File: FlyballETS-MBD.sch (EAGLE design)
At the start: 16 parts, among them Q1 BC557, Q2 BC557

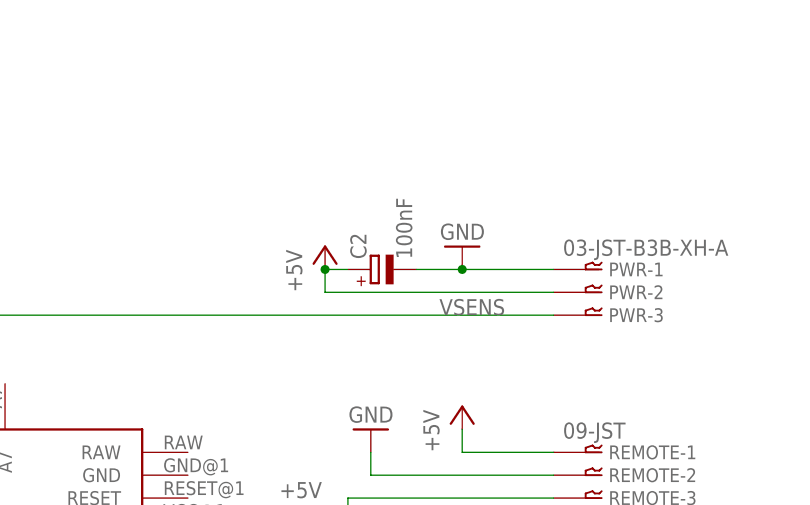
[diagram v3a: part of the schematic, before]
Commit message: Incorrect capacitor value
Changed 100nF to 100uF
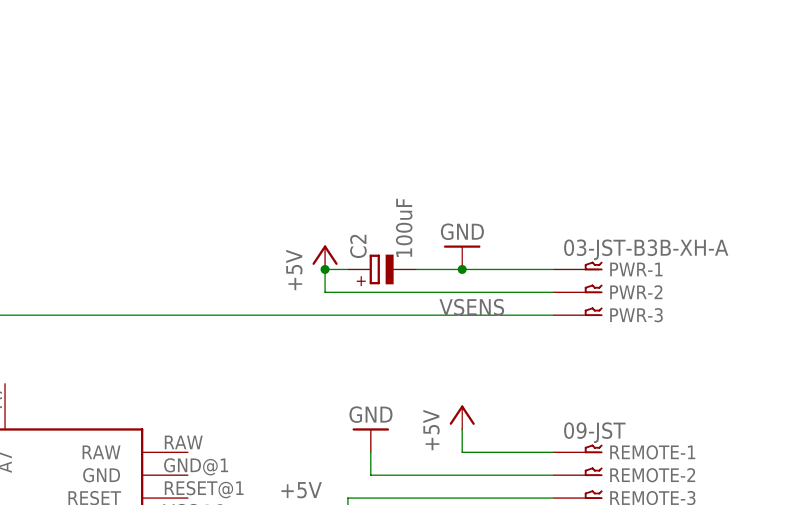
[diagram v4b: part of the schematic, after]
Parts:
- C2: value 100nF -> 100uF
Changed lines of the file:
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@@
 <part name="P+2" library="supply1" deviceset="+5V" device=""/>
 <part name="GND7" library="supply1" deviceset="GND" device=""/>
-<part name="C2" library="resistor" deviceset="CPOL-EU" device="E2,5-6E" value="100nF"/>
+<part name="C2" library="resistor" deviceset="CPOL-EU" device="E2,5-6E" value="100uF"/>
 <part name="ARDUINO" library="_custom" deviceset="ARDPROMINISOCK" device=""/>
 <part name="FRAME1" library="frames" deviceset="A4L-LOC" device=""/>

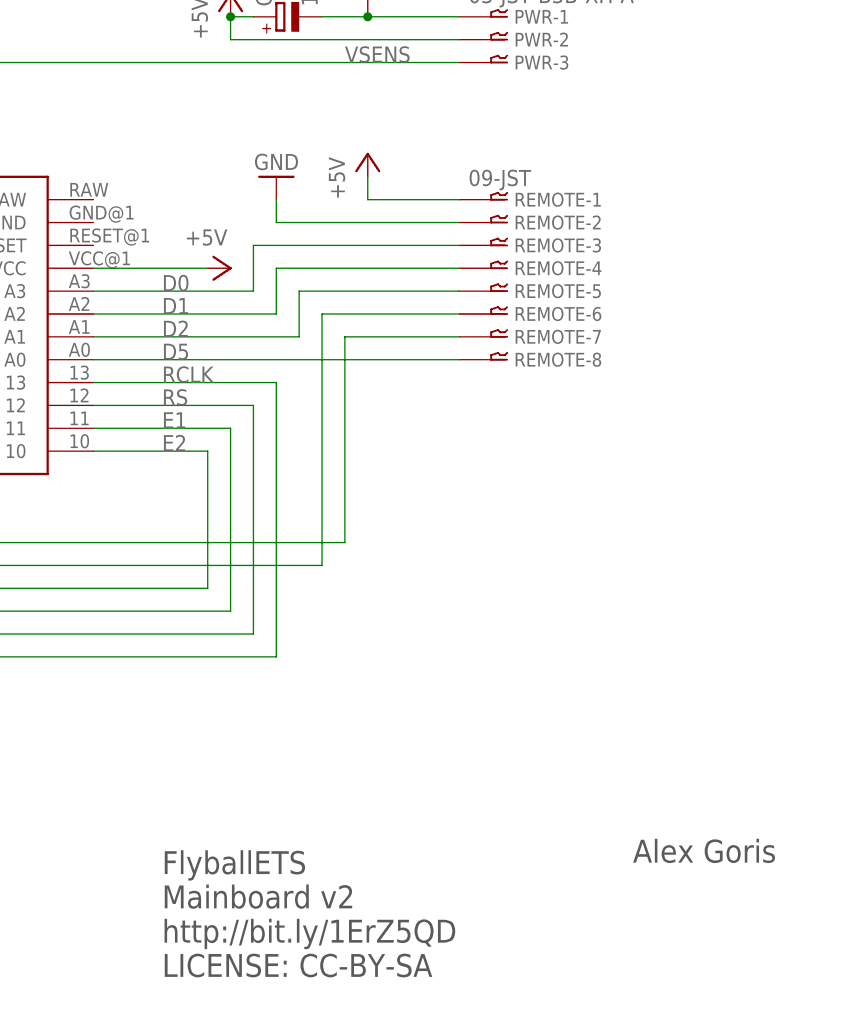
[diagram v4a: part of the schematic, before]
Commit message: Fixed JST XH pin numbering
Updated bt_con-jst-xh.lbr library with swapped pin numbering.
Updated all board designs with updated library so they have the
connectors the right way around
Fixes #4
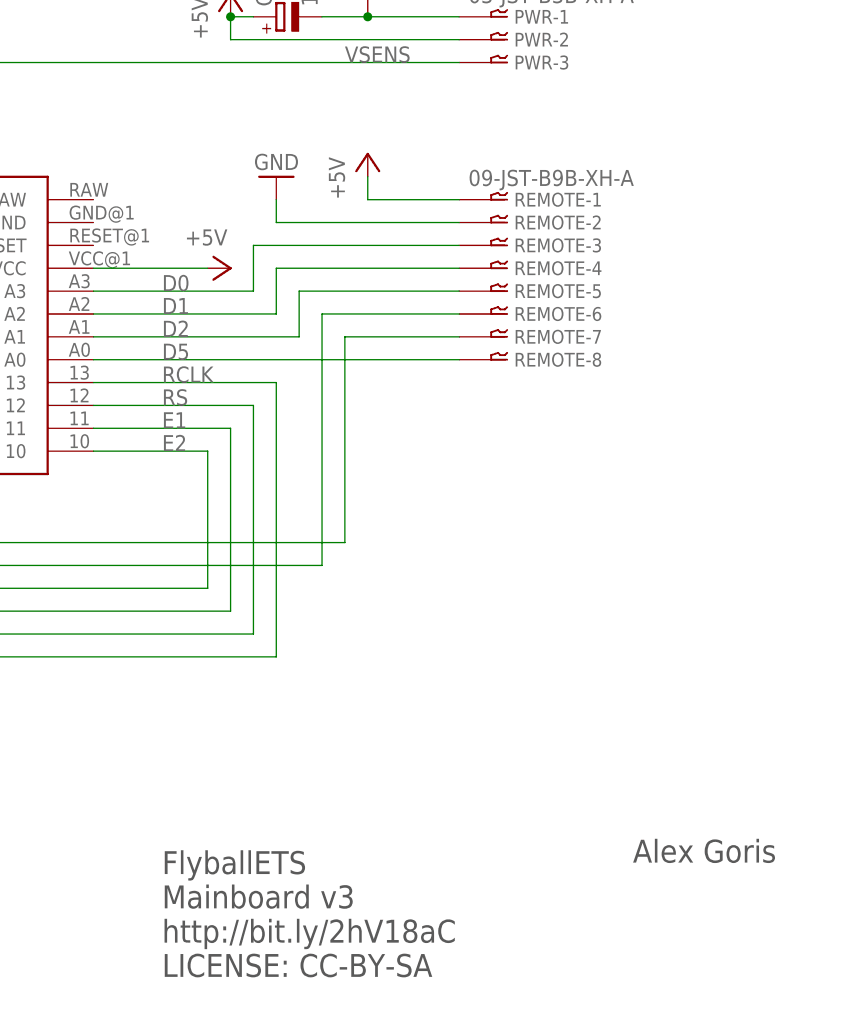
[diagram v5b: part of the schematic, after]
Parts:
- REMOTE: value 09-JST -> 09-JST-B9B-XH-A; device bt_con-jst-xh:09-JST -> bt_con-jst-xh:09-JST-B9B-XH-A
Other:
- note added: "FlyballETS Mainboard v3 http://bit.ly/2hV18aC LICENSE: CC-BY-SA"
- note removed: "FlyballETS Mainboard v2 http://bit.ly/1ErZ5QD LICENSE: CC-BY-SA"
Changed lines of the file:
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@@
 <?xml version="1.0" encoding="utf-8"?>
 <!DOCTYPE eagle SYSTEM "eagle.dtd">
-<eagle version="7.5.0">
+<eagle version="8.2.2">
 <drawing>
 <settings>
@@
 <part name="PWR" library="bt_con-jst-xh" deviceset="03-JST" device="-B3B-XH-A"/>
 <part name="SENS" library="bt_con-jst-xh" deviceset="02-JST" device=""/>
-<part name="REMOTE" library="bt_con-jst-xh" deviceset="09-JST" device=""/>
+<part name="REMOTE" library="bt_con-jst-xh" deviceset="09-JST" device="-B9B-XH-A"/>
 </parts>
 <sheets>
@@
 <text x="50.8" y="35.56" size="1.778" layer="97">LCD</text>
 <text x="127" y="17.78" size="2.54" layer="97">FlyballETS
-Mainboard v2
-http://bit.ly/1ErZ5QD
+Mainboard v3
+http://bit.ly/2hV18aC
 LICENSE: CC-BY-SA</text>
 <text x="179.324" y="30.48" size="2.54" layer="97">Alex Goris</text>
